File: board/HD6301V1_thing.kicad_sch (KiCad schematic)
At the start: 45 parts, among them J1 KMDGX-6S-BS, J2 ps2_i2c, J3 P1_connector, J4 memmap_i2c, J5 8bit_thing_bus_connector, J6 USB_B_Micro, J7 prog_LED, J8 pwr_LED, SW1 Reset, SW2 Banking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

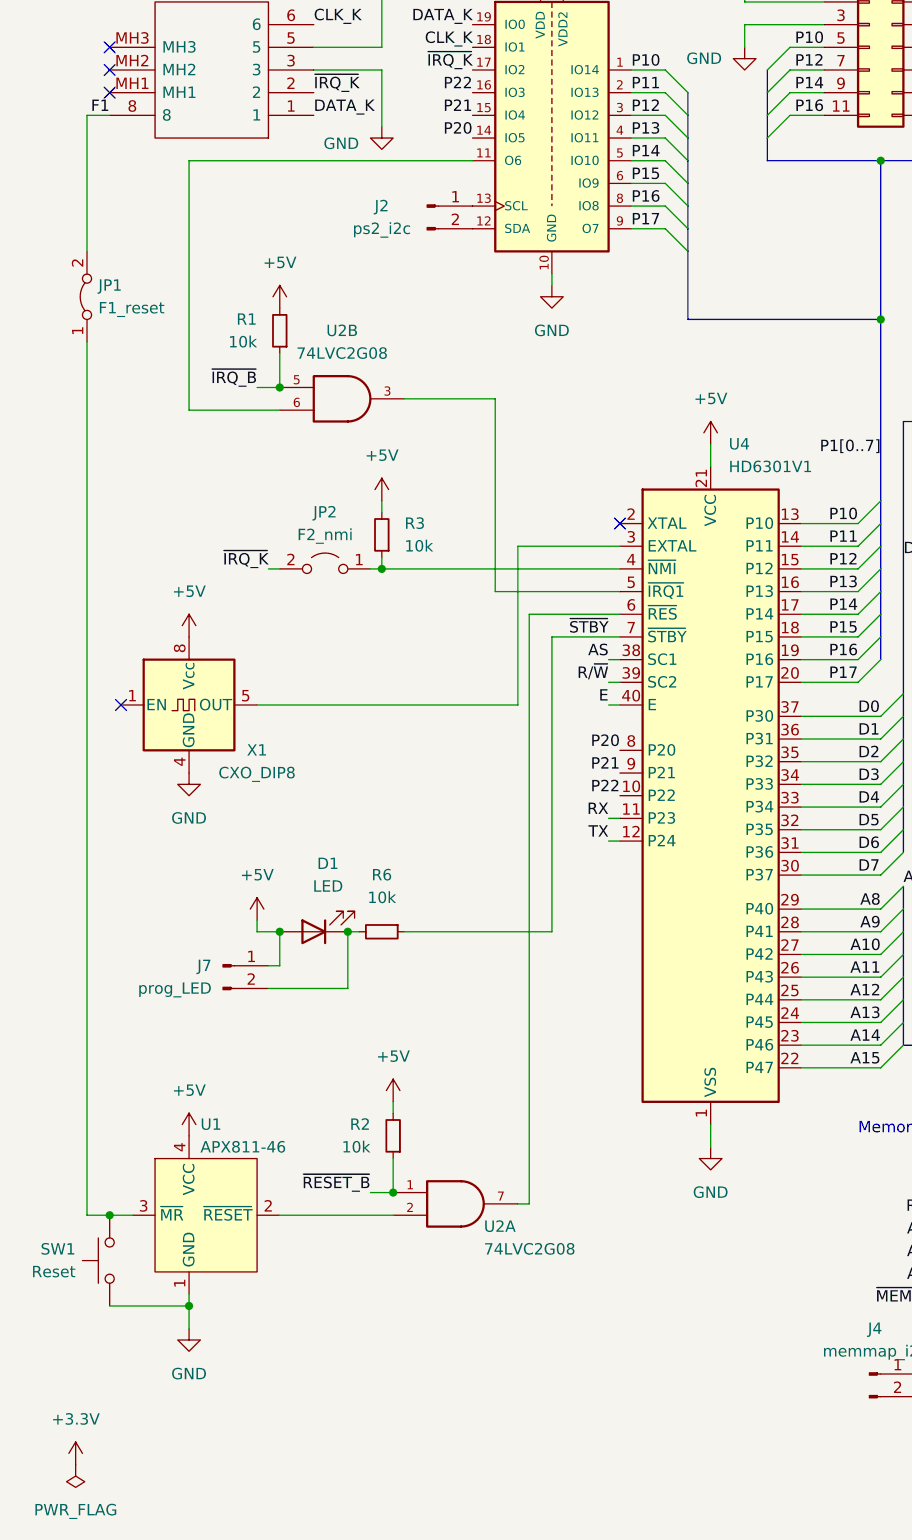
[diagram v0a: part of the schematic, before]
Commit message: Replace IRQ/RESET AND IC with a Schmitt-trigger one
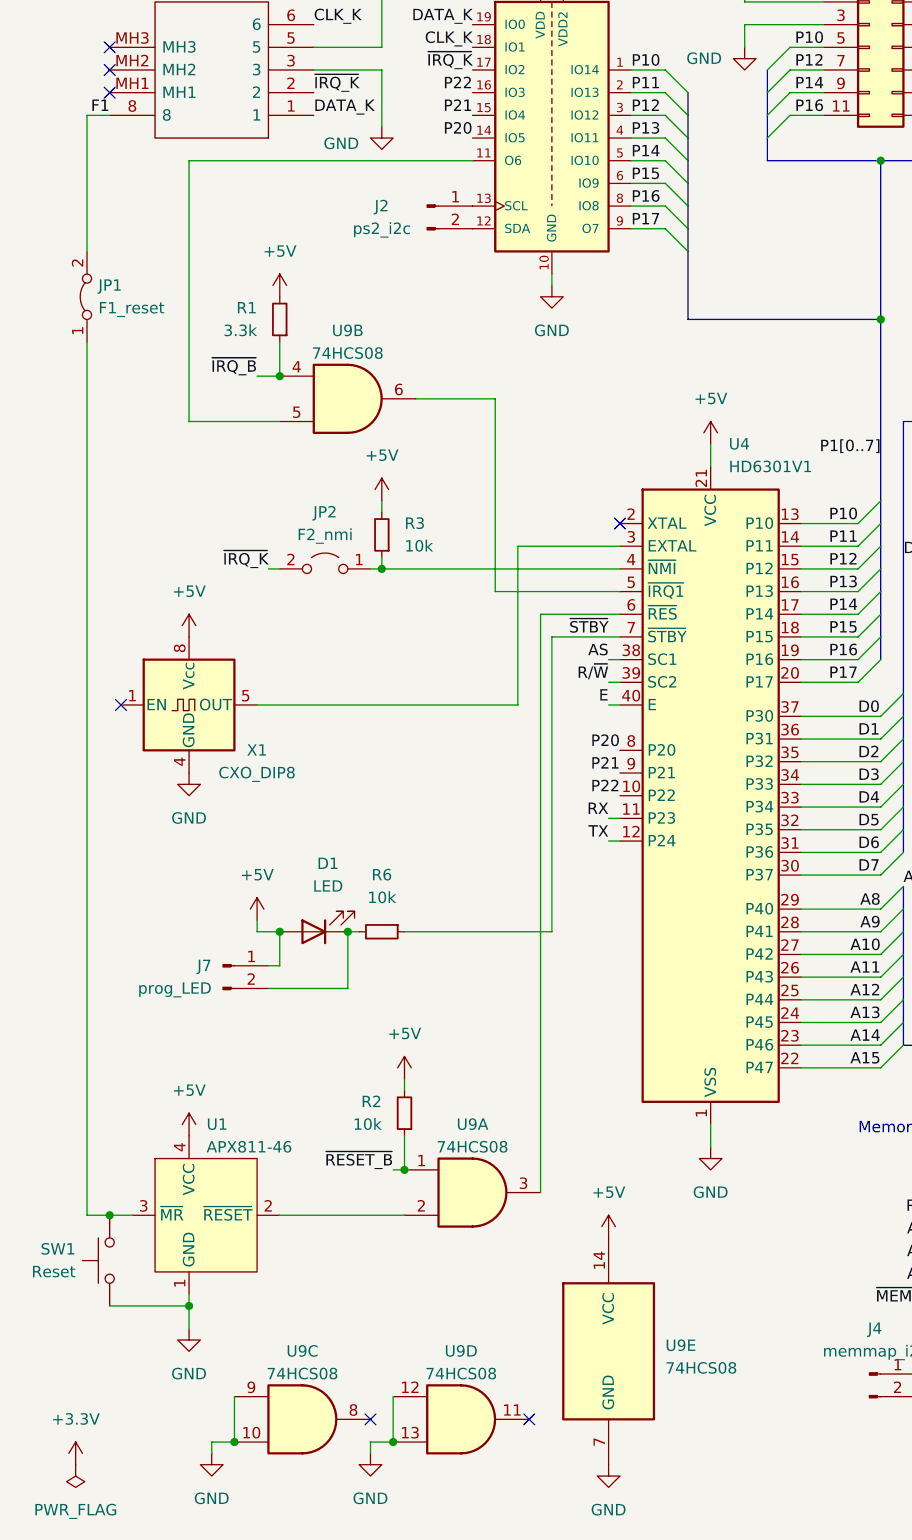
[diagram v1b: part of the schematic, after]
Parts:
- removed U2: 74LVC2G08, Package_SO:VSSOP-8_2.3x2mm_P0.5mm, symbol own_symbols:74LVC2G08_5V_power
- added U9: 74HCS08, Package_SO:TSSOP-14_4.4x5mm_P0.65mm, symbol 74xx:74LS08
- R1: value 10k -> 3.3k
- U3, U5: footprint SOP65P640X120-20N -> imported_footprints:SOP65P640X120-20N
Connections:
- net +5V: now also U9.14 (VCC)
- net GND: now also U9.10, U9.12, U9.13, U9.7 (GND), U9.9
- net ~{IRQ_B}: now also U9.4
- net ~{RESET_B}: now also U9.1
- net at U4.5 (~{IRQ1}): now also U9.6
- net at U3.11 (O6): now also U9.5
- net at U1.2 (~{RESET}): now also U9.2
- net at U4.6 (~{RES}): now also U9.3
- no-connect marks 11 -> 13
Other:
- moved on the sheet: R1, R2

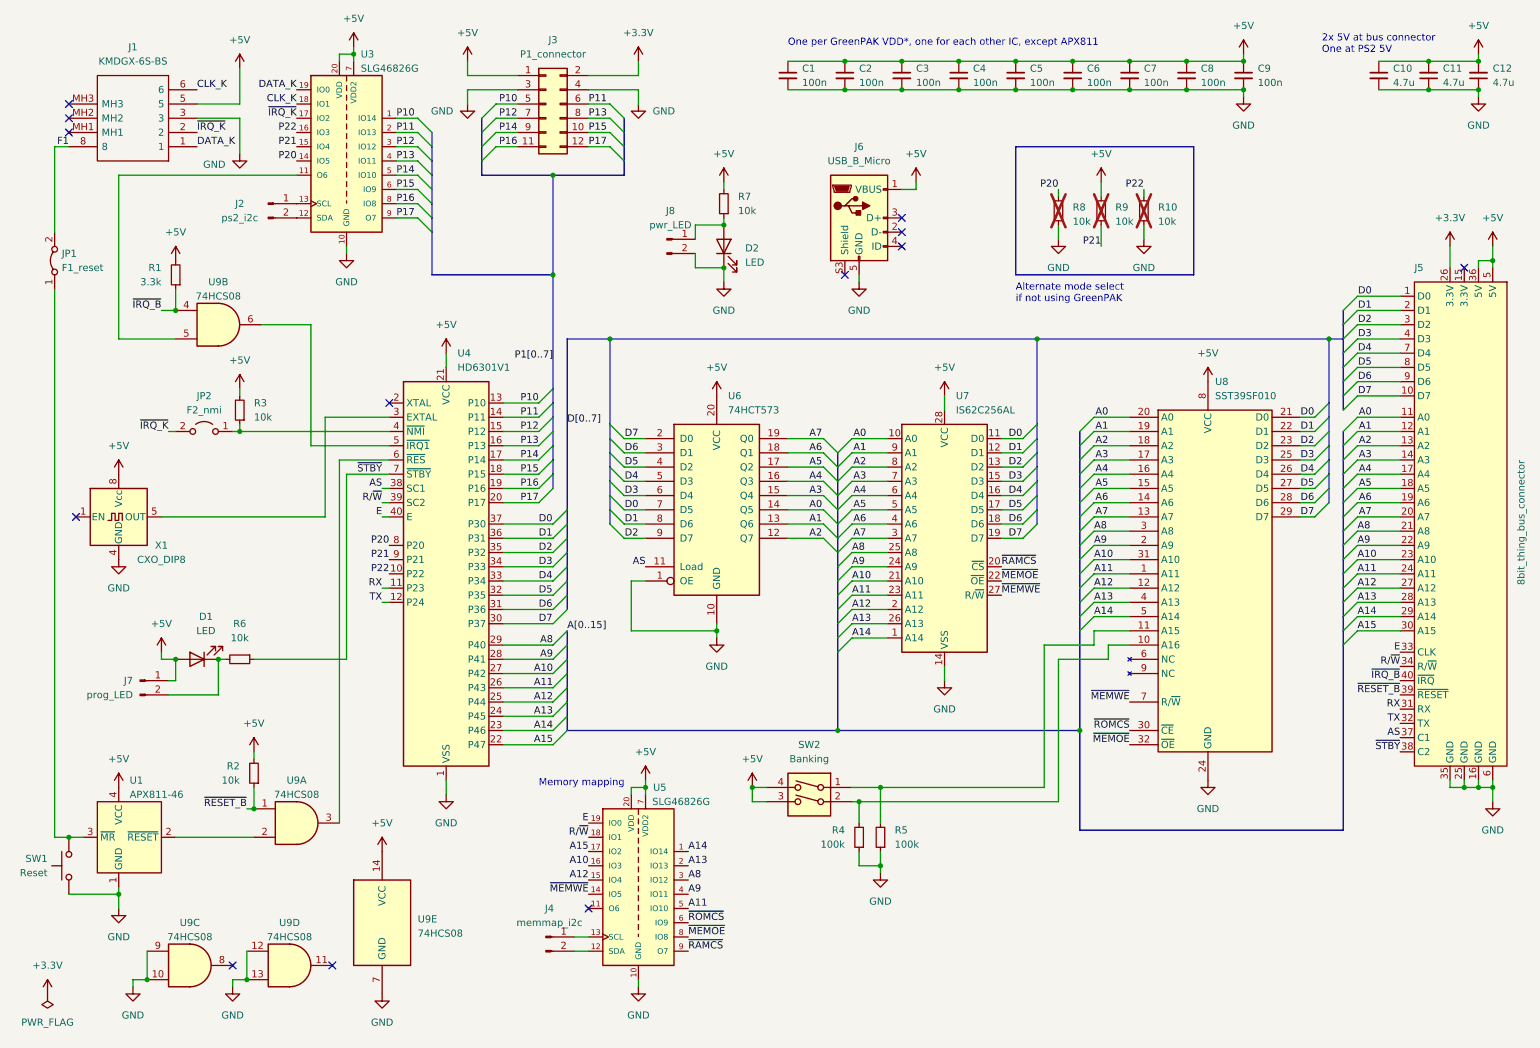
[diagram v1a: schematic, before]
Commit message: Fix missing pullup on STBYB
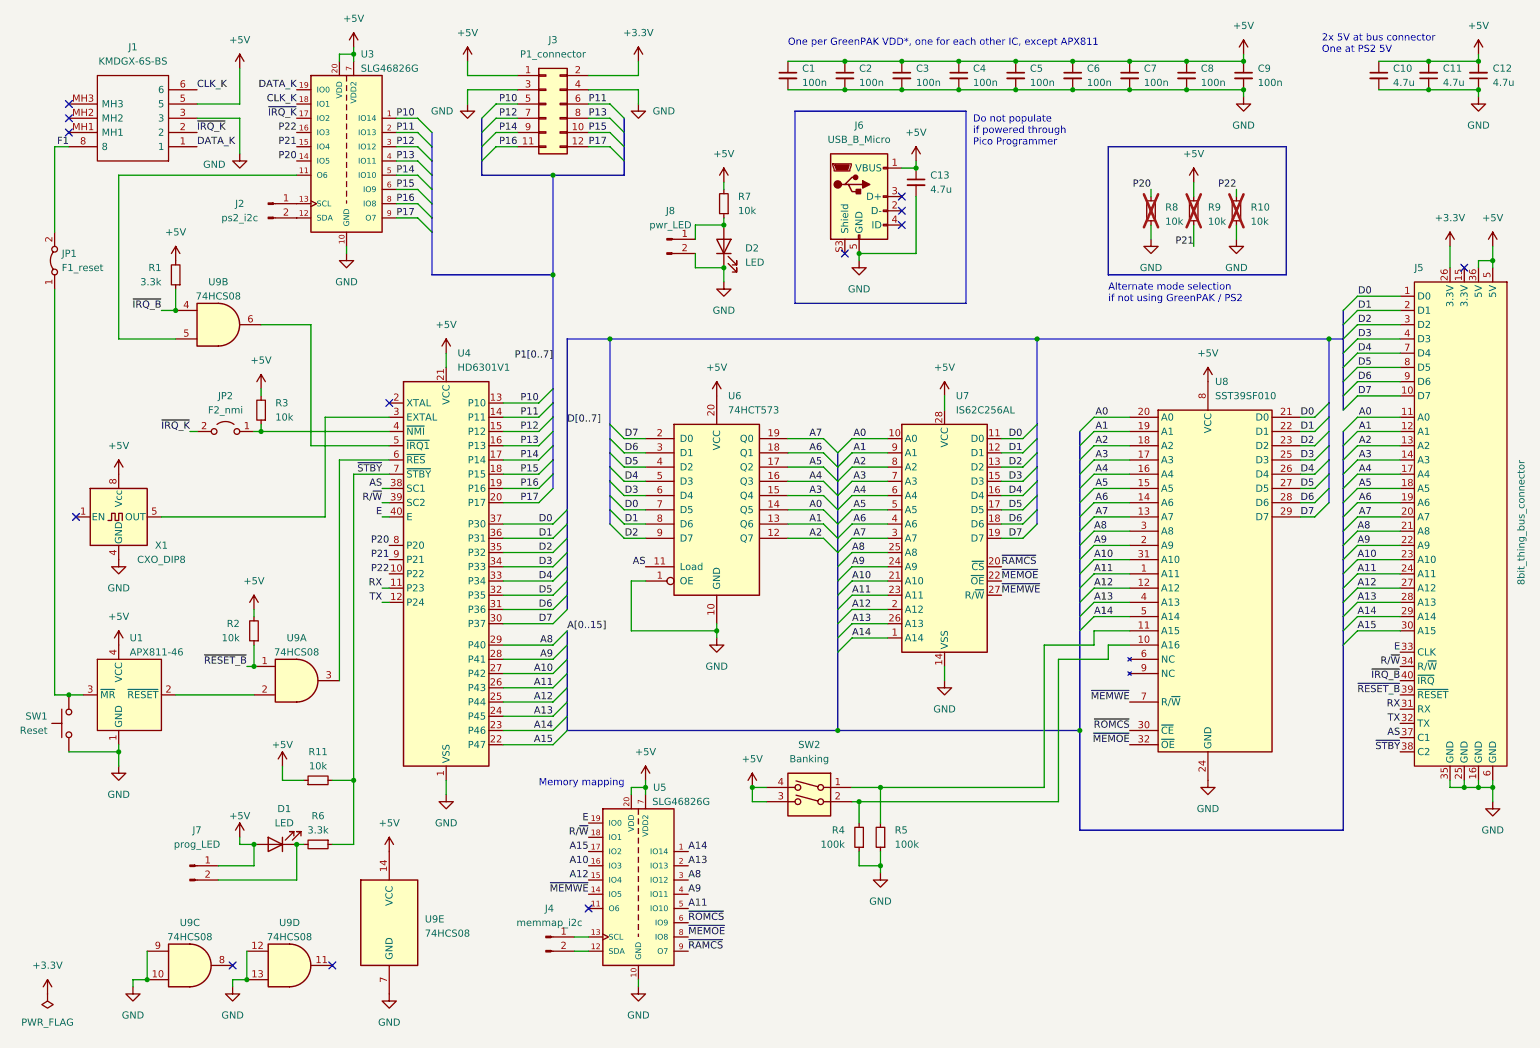
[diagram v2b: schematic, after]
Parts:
- added C13: 4.7u, Capacitor_SMD:C_0805_2012Metric_Pad1.18x1.45mm_HandSolder, symbol Device:C_Small
- added R11: 10k, Resistor_SMD:R_0805_2012Metric_Pad1.20x1.40mm_HandSolder, symbol Device:R_Small
- R6: value 10k -> 3.3k
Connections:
- net +5V: now also C13.1, R11.1
- net GND: now also C13.2
- net ~{STBY}: now also R11.2
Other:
- note added: "Alternate mode selection if not using GreenPAK / PS2"
- note added: "Do not populate if powered through Pico Programmer"
- note removed: "Alternate mode select if not using GreenPAK"
- moved on the sheet: D1, J6, J7, JP2, R10, R2, R3, R6, R8, R9, SW1, U1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

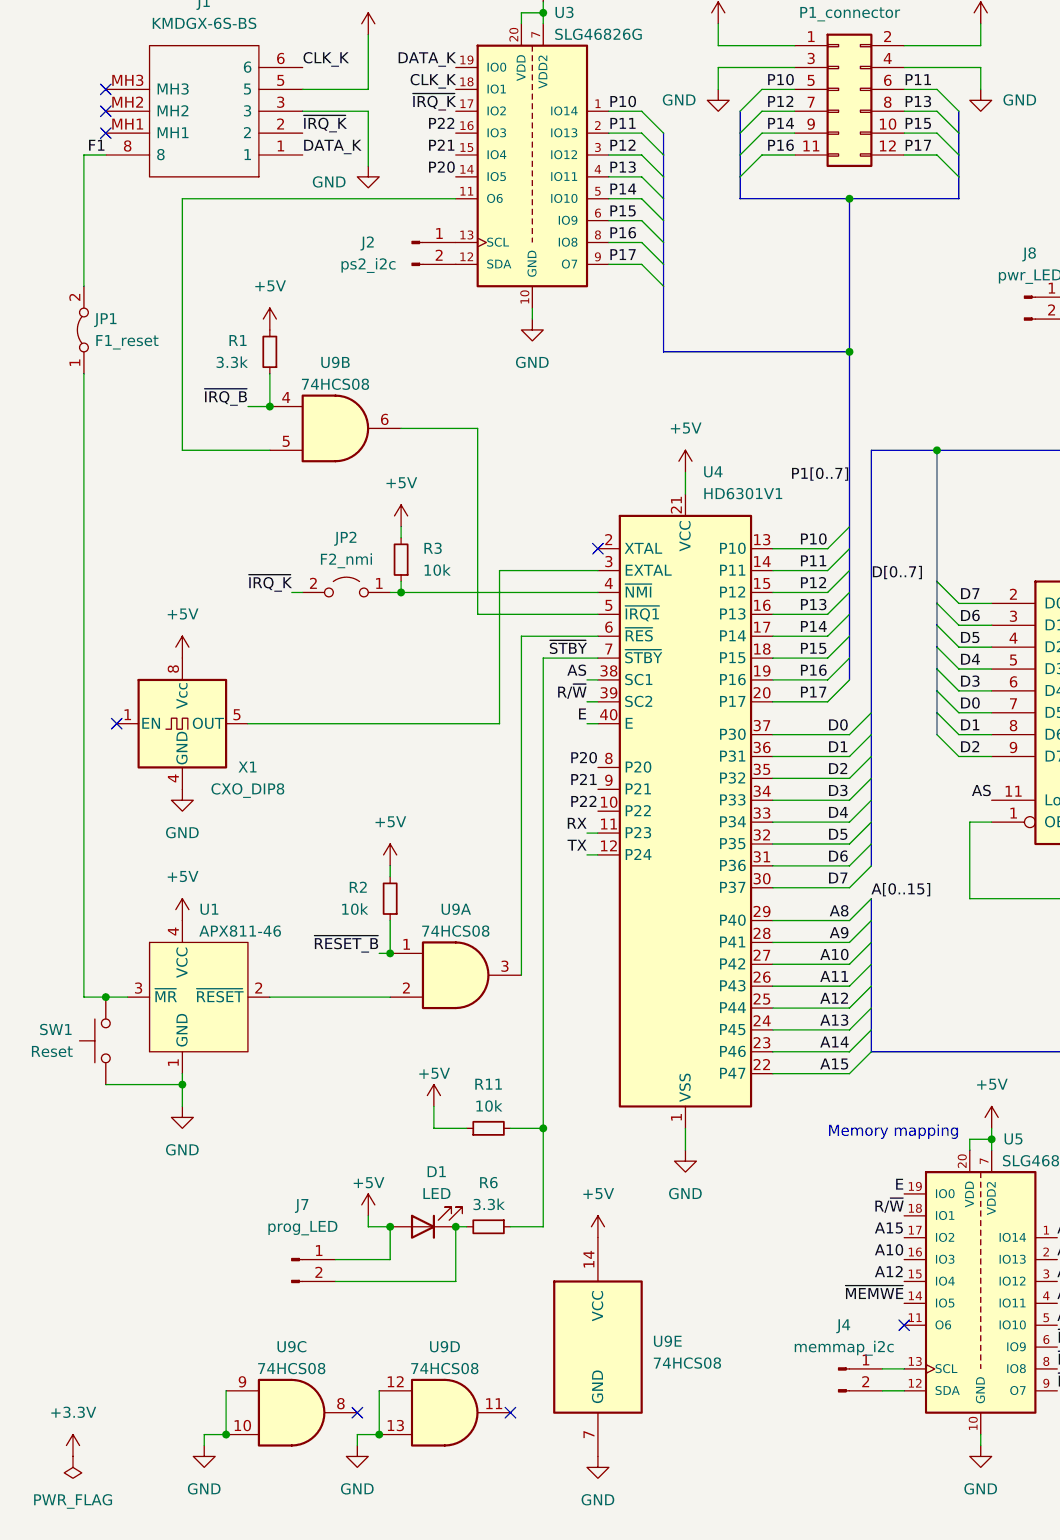
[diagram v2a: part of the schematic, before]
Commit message: HD6301 board: add GreenPAK i2c pullups
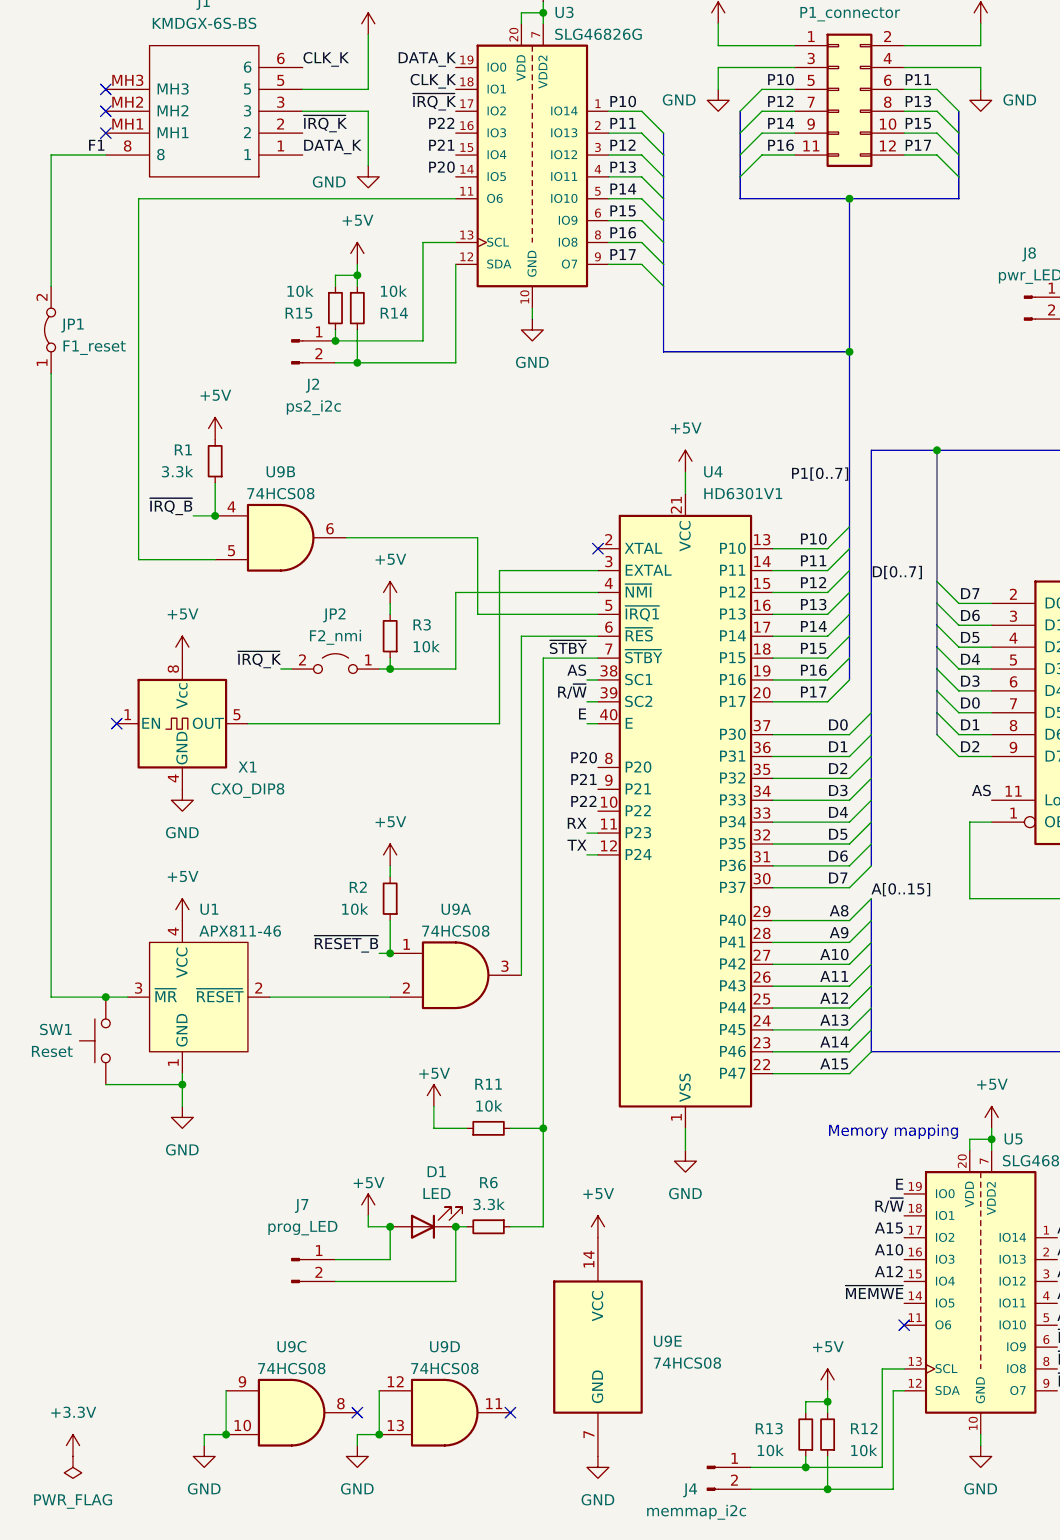
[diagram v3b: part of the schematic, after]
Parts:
- added R12, R13, R14, R15: 10k, Resistor_SMD:R_0805_2012Metric_Pad1.20x1.40mm_HandSolder, symbol Device:R_Small
- J2, J4: footprint Connector_PinHeader_2.54mm:PinHeader_1x02_P2.54mm_Vertical -> own_footprints:PinHeader_1x02_P2.54mm_Vertical_minimal
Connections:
- net +5V: now also R12.2, R13.2, R14.1, R15.1
- net at J2.2 (Pin_2), U3.12 (SDA): now also R14.2
- net at J2.1 (Pin_1), U3.13 (SCL): now also R15.2
- net at J4.1 (Pin_1), U5.13 (SCL): now also R13.1
- net at J4.2 (Pin_2), U5.12 (SDA): now also R12.1
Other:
- moved on the sheet: J2, J4, JP1, JP2, R1, R3, U9B
